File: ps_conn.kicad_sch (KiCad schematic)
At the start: 1 part, among them J2 61082-061400LF

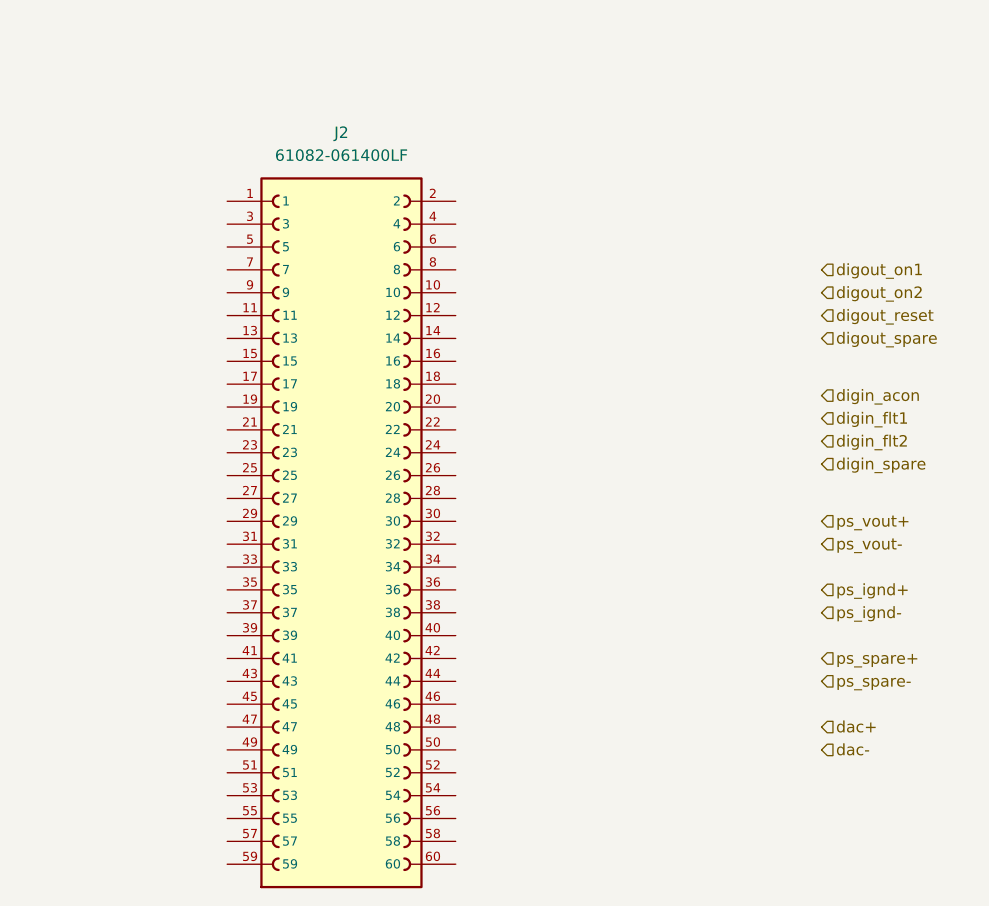
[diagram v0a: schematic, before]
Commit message: Add DCCT ADCs
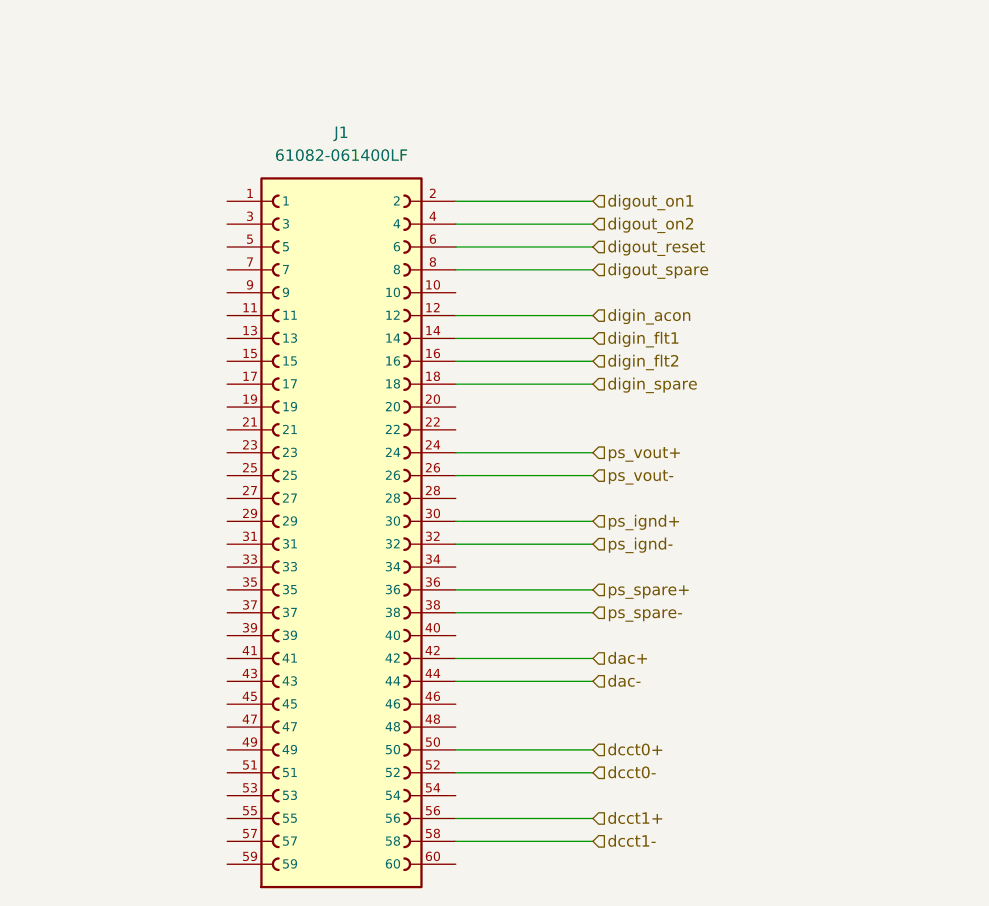
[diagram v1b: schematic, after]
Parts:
- renumbered J2 to J1
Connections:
- net dac+: now also J1.42
- net dac-: now also J1.44
- net digin_acon: now also J1.12
- net digin_flt1: now also J1.14
- net digin_flt2: now also J1.16
- net digin_spare: now also J1.18
- net digout_on1: now also J1.2
- net digout_on2: now also J1.4
- net digout_reset: now also J1.6
- net digout_spare: now also J1.8
- net ps_ignd+: now also J1.30
- net ps_ignd-: now also J1.32
- net ps_spare+: now also J1.36
- net ps_spare-: now also J1.38
- net ps_vout+: now also J1.24
- net ps_vout-: now also J1.26
- net dcct0+: now reaches J1.50
- net dcct0-: now reaches J1.52
- net dcct1+: now reaches J1.56
- net dcct1-: now reaches J1.58

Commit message: DAC and DCCT placement
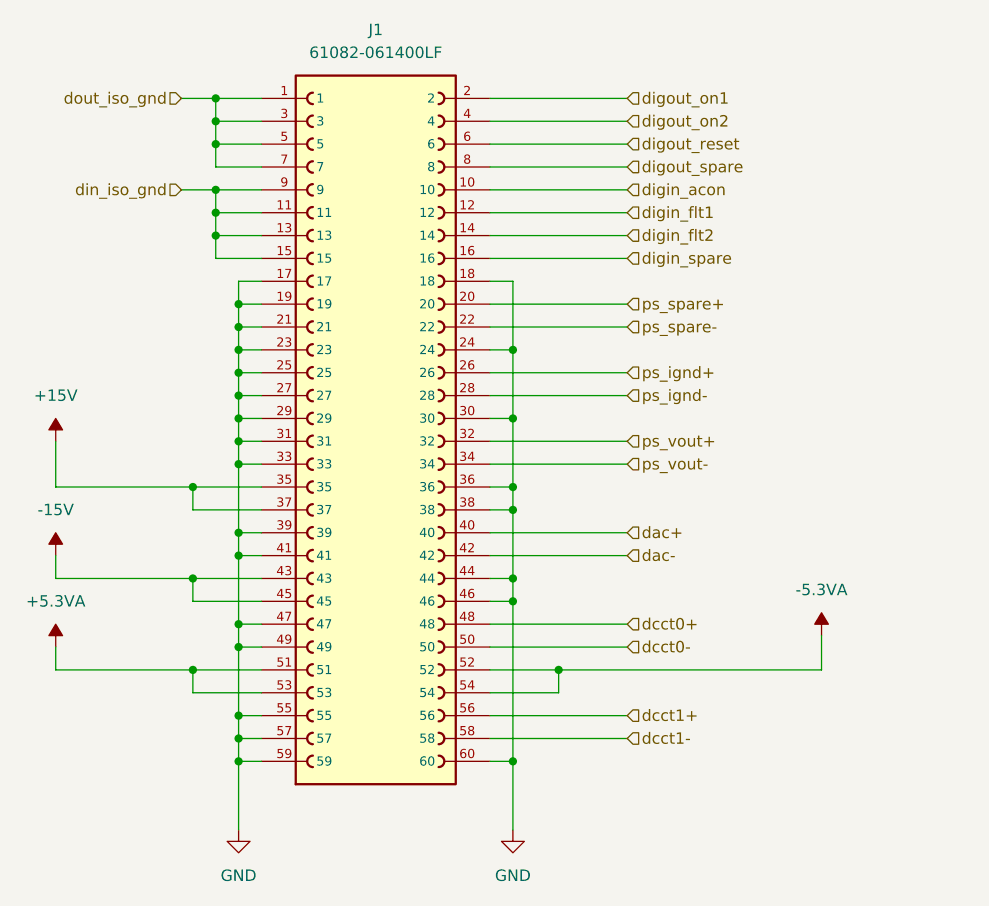
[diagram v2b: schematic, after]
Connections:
- net dac+: now also J1.40; no longer J1.42
- net dac-: now also J1.42; no longer J1.44
- net dcct0+: now also J1.48; no longer J1.50
- net dcct0-: now also J1.50; no longer J1.52
- net digin_acon: now also J1.10; no longer J1.12
- net digin_flt1: now also J1.12; no longer J1.14
- net digin_flt2: now also J1.14; no longer J1.16
- net digin_spare: now also J1.16; no longer J1.18
- net ps_ignd+: now also J1.26; no longer J1.30
- net ps_ignd-: now also J1.28; no longer J1.32
- net ps_spare+: now also J1.20; no longer J1.36
- net ps_spare-: now also J1.22; no longer J1.38
- net ps_vout+: now also J1.32; no longer J1.24
- net ps_vout-: now also J1.34; no longer J1.26
- net dout_iso_gnd: now reaches J1.1
- net dout_iso_gnd: now also J1.3, J1.5, J1.7
- net din_iso_gnd: now reaches J1.11
- net din_iso_gnd: now also J1.13, J1.15, J1.9
- net GND: now reaches J1.17
- net GND: now also J1.18, J1.19, J1.21, J1.23, J1.24, J1.25, J1.27, J1.29, J1.30, J1.31, J1.33, J1.36, J1.38, J1.39, J1.41, J1.44, J1.46, J1.47, J1.49, J1.55, J1.57, J1.59, J1.60
- net +15V: now reaches J1.35
- net +15V: now also J1.37
- net -15V: now reaches J1.43
- net -15V: now also J1.45
- net +5.3VA: now reaches J1.51
- net +5.3VA: now also J1.53
- net -5.3VA: now reaches J1.54
- net -5.3VA: now also J1.52
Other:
- moved on the sheet: J1

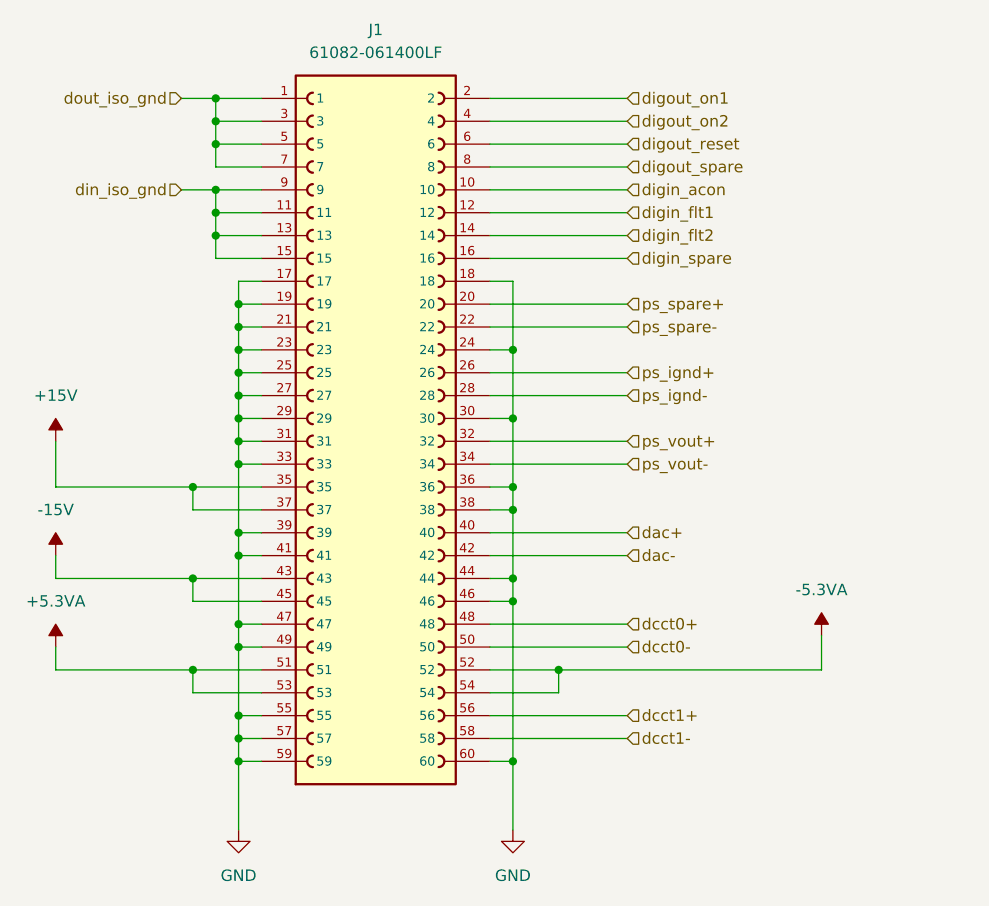
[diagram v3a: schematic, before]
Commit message: Tweaks to connector pinouts
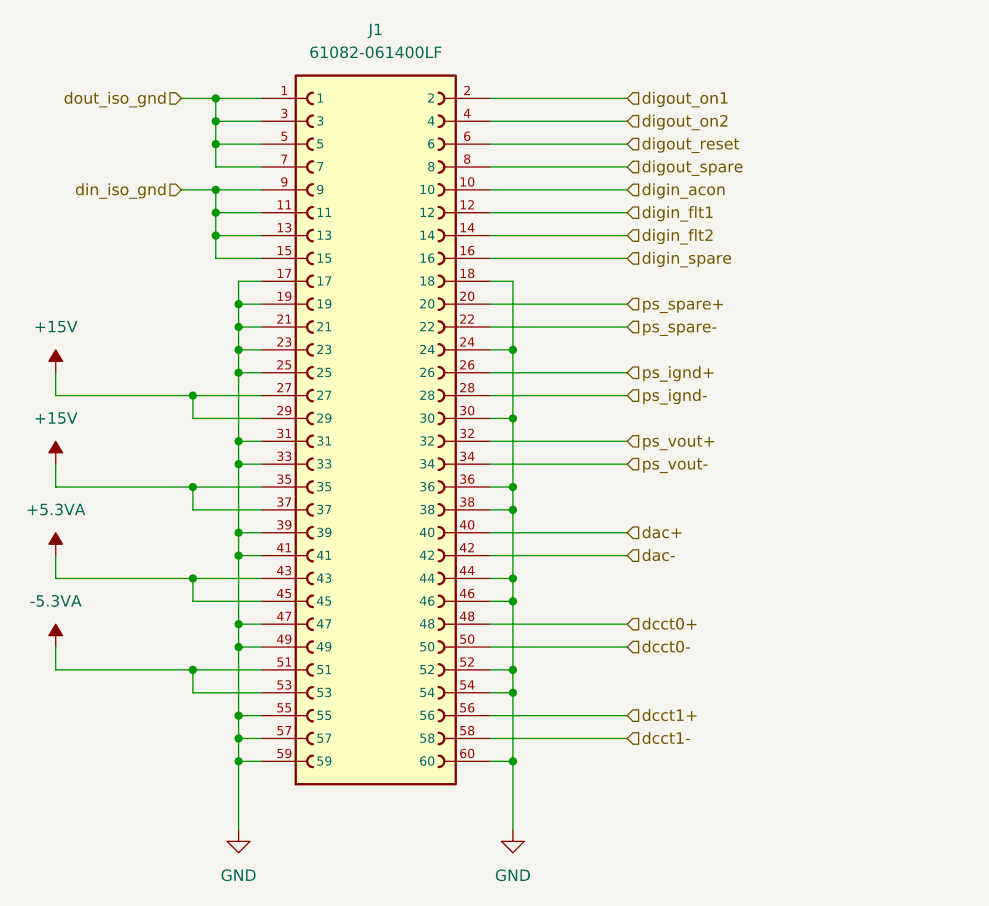
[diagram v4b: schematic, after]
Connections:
- net -15V is gone; now on net +5.3VA: J1.43, J1.45
- net +15V: now also J1.27, J1.29
- net +5.3VA: no longer J1.51, J1.53
- net -5.3VA: now also J1.51, J1.53; no longer J1.52, J1.54
- net GND: now also J1.52, J1.54; no longer J1.27, J1.29

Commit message: Finish layout
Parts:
- J1: Cost (none) -> 2.53; MFG (none) -> Amphenol; MFG_PN (none) -> 61082-061400LF
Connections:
- net +15V: no longer J1.35, J1.37
- net digin_acon: now also J1.16; no longer J1.10
- net digin_flt1: now also J1.14; no longer J1.12
- net digin_flt2: now also J1.12; no longer J1.14
- net digin_spare: now also J1.10; no longer J1.16
- net digout_on1: now also J1.8; no longer J1.2
- net digout_on2: now also J1.6; no longer J1.4
- net digout_reset: now also J1.4; no longer J1.6
- net digout_spare: now also J1.2; no longer J1.8
- net din_iso_gnd: now also J1.1, J1.3, J1.5, J1.7; no longer J1.11, J1.13, J1.15, J1.9
- net dout_iso_gnd: now also J1.11, J1.13, J1.15, J1.9; no longer J1.1, J1.3, J1.5, J1.7
- new net -15V: J1.35, J1.37
